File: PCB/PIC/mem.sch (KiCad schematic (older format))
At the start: 14 parts, among them U12 24AA1025, U13 24AA025E48

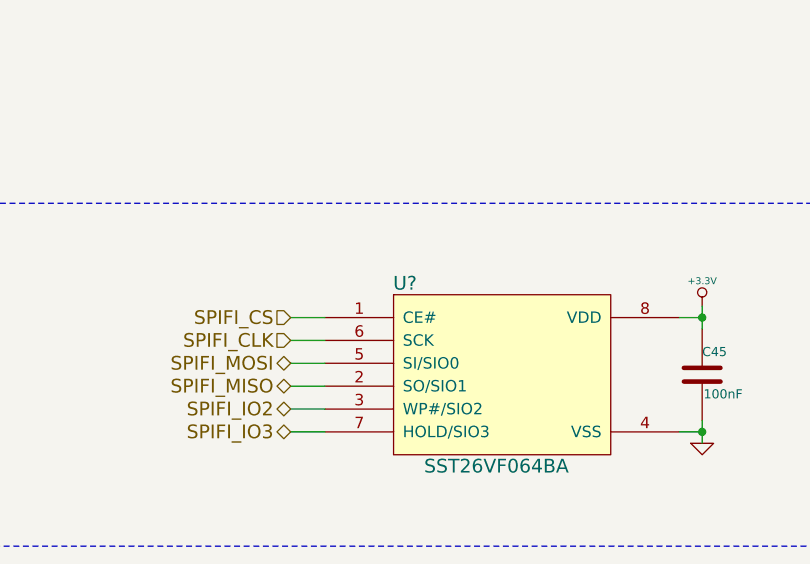
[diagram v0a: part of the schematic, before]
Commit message: CIAA PIC correccion FT232RL
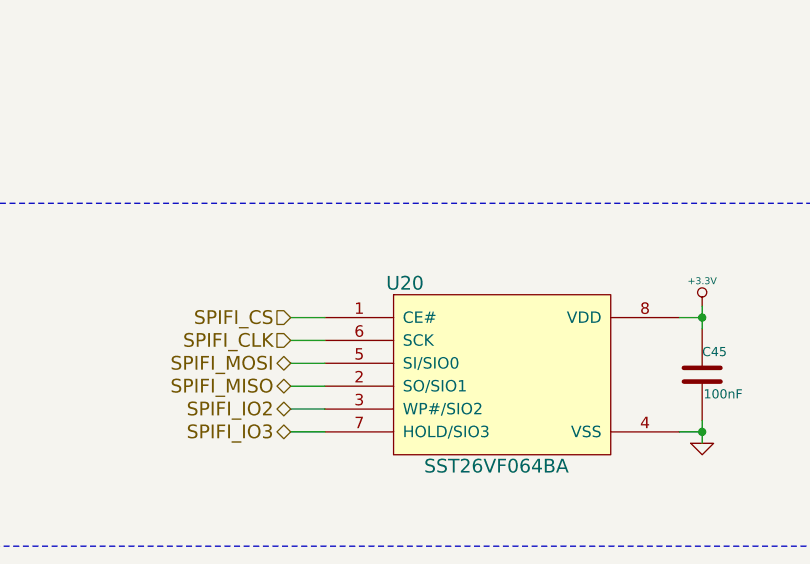
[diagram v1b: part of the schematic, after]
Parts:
- gave numbers to parts that had none: 1
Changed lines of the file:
@@
 Sheet 9 12
 Title "CIAA micro SD card"
-Date "19 dec 2014"
+Date "29 dec 2014"
 Rev "1.0"
 Comp ""
@@
 I2C_SCL
 $Comp
-L GND #PWR164
+L GND #PWR163
 U 1 1 52E536B1
 P 3800 2600
-F 0 "#PWR164" H 3800 2600 30  0001 C CNN
+F 0 "#PWR163" H 3800 2600 30  0001 C CNN
 F 1 "GND" H 3800 2530 30  0001 C CNN
 F 2 "" H 3800 2600 60  0000 C CNN
@@
 $EndComp
 $Comp
-L +3.3V #PWR163
+L +3.3V #PWR162
 U 1 1 52E536B7
 P 3800 1150
-F 0 "#PWR163" H 3800 1110 30  0001 C CNN
+F 0 "#PWR162" H 3800 1110 30  0001 C CNN
 F 1 "+3.3V" H 3800 1260 30  0000 C CNN
 F 2 "" H 3800 1150 60  0000 C CNN
@@
 $EndComp
 $Comp
-L GND #PWR161
+L GND #PWR160
 U 1 1 52E536C5
 P 2850 2600
-F 0 "#PWR161" H 2850 2600 30  0001 C CNN
+F 0 "#PWR160" H 2850 2600 30  0001 C CNN
 F 1 "GND" H 2850 2530 30  0001 C CNN
 F 2 "" H 2850 2600 60  0000 C CNN
@@
 $EndComp
 $Comp
-L GND #PWR160
+L GND #PWR159
 U 1 1 52E536CB
 P 2700 2600
-F 0 "#PWR160" H 2700 2600 30  0001 C CNN
+F 0 "#PWR159" H 2700 2600 30  0001 C CNN
 F 1 "GND" H 2700 2530 30  0001 C CNN
 F 2 "" H 2700 2600 60  0000 C CNN
@@
 $EndComp
 $Comp
-L GND #PWR165
+L GND #PWR164
 U 1 1 52E536D1
 P 4150 1650
-F 0 "#PWR165" H 4150 1650 30  0001 C CNN
+F 0 "#PWR164" H 4150 1650 30  0001 C CNN
 F 1 "GND" H 4150 1580 30  0001 C CNN
 F 2 "" H 4150 1650 60  0000 C CNN
@@
 $EndComp
 $Comp
-L GND #PWR166
+L GND #PWR165
 U 1 1 52E536DF
 P 4850 1550
-F 0 "#PWR166" H 4850 1550 30  0001 C CNN
+F 0 "#PWR165" H 4850 1550 30  0001 C CNN
 F 1 "GND" H 4850 1480 30  0001 C CNN
 F 2 "" H 4850 1550 60  0000 C CNN
@@
 $EndComp
 $Comp
-L +3.3V #PWR162
+L +3.3V #PWR161
 U 1 1 52E536E8
 P 3000 2600
-F 0 "#PWR162" H 3000 2560 30  0001 C CNN
+F 0 "#PWR161" H 3000 2560 30  0001 C CNN
 F 1 "+3.3V" H 3000 2710 30  0000 C CNN
 F 2 "" H 3000 2600 60  0000 C CNN
@@
 I2C_SCL
 $Comp
-L GND #PWR173
+L GND #PWR172
 U 1 1 52E536F8
 P 8100 2600
-F 0 "#PWR173" H 8100 2600 30  0001 C CNN
+F 0 "#PWR172" H 8100 2600 30  0001 C CNN
 F 1 "GND" H 8100 2530 30  0001 C CNN
 F 2 "" H 8100 2600 60  0000 C CNN
@@
 $EndComp
 $Comp
-L +3.3V #PWR172
+L +3.3V #PWR171
 U 1 1 52E536FE
 P 8100 1150
-F 0 "#PWR172" H 8100 1110 30  0001 C CNN
+F 0 "#PWR171" H 8100 1110 30  0001 C CNN
 F 1 "+3.3V" H 8100 1260 30  0000 C CNN
 F 2 "" H 8100 1150 60  0000 C CNN
@@
 $EndComp
 $Comp
-L GND #PWR168
+L GND #PWR169
 U 1 1 52E5370C
 P 7150 2600
-F 0 "#PWR168" H 7150 2600 30  0001 C CNN
+F 0 "#PWR169" H 7150 2600 30  0001 C CNN
 F 1 "GND" H 7150 2530 30  0001 C CNN
 F 2 "" H 7150 2600 60  0000 C CNN
@@
 $EndComp
 $Comp
-L GND #PWR174
+L GND #PWR173
 U 1 1 52E53712
 P 8450 1650
-F 0 "#PWR174" H 8450 1650 30  0001 C CNN
+F 0 "#PWR173" H 8450 1650 30  0001 C CNN
 F 1 "GND" H 8450 1580 30  0001 C CNN
 F 2 "" H 8450 1650 60  0000 C CNN
@@
 $EndComp
 $Comp
-L GND #PWR175
+L GND #PWR174
 U 1 1 52E5371B
 P 9150 1550
-F 0 "#PWR175" H 9150 1550 30  0001 C CNN
+F 0 "#PWR174" H 9150 1550 30  0001 C CNN
 F 1 "GND" H 9150 1480 30  0001 C CNN
 F 2 "" H 9150 1550 60  0000 C CNN
@@
 $EndComp
 $Comp
-L +3.3V #PWR167
+L +3.3V #PWR168
 U 1 1 52E53724
 P 7000 2600
-F 0 "#PWR167" H 7000 2560 30  0001 C CNN
+F 0 "#PWR168" H 7000 2560 30  0001 C CNN
 F 1 "+3.3V" H 7000 2710 30  0000 C CNN
 F 2 "" H 7000 2600 60  0000 C CNN
@@
 $EndComp
 $Comp
-L GND #PWR169
+L GND #PWR170
 U 1 1 52E5372A
 P 7300 2600
-F 0 "#PWR169" H 7300 2600 30  0001 C CNN
+F 0 "#PWR170" H 7300 2600 30  0001 C CNN
 F 1 "GND" H 7300 2530 30  0001 C CNN
 F 2 "" H 7300 2600 60  0000 C CNN
@@
 $EndComp
 $Comp
-L +3.3V #PWR170
+L +3.3V #PWR166
 U 1 1 52E5407E
 P 6700 4300
-F 0 "#PWR170" H 6700 4260 30  0001 C CNN
+F 0 "#PWR166" H 6700 4260 30  0001 C CNN
 F 1 "+3.3V" H 6700 4410 30  0000 C CNN
 F 2 "" H 6700 4300 60  0000 C CNN
@@
 $EndComp
 $Comp
-L GND #PWR171
+L GND #PWR167
 U 1 1 52E540A7
 P 6700 4900
-F 0 "#PWR171" H 6700 4900 30  0001 C CNN
+F 0 "#PWR167" H 6700 4900 30  0001 C CNN
 F 1 "GND" H 6700 4830 30  0001 C CNN
 F 2 "" H 6700 4900 60  0000 C CNN
@@
 Flash QSPI, 64Mbit
 $Comp
-L SST26VF064BA U?
+L SST26VF064BA U20
 U 1 1 5493BBA5
 P 5800 4600
-F 0 "U?" H 5400 5000 60  0000 C CNN
+F 0 "U20" H 5400 5000 60  0000 C CNN
 F 1 "SST26VF064BA" H 5800 4200 60  0000 C CNN
 F 2 "~" H 5800 4400 60  0000 C CNN

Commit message: Correcciones al esquematico segun rev01
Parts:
- added U?: 23A1024, footprints:-SOIC8, symbol 23A1024
- C19, C20, C45: symbol C -> C-RESCUE-ciaa-pic
- R23, R24, R25, R26, R27, R28, R29, R30: symbol R -> R-RESCUE-ciaa-pic
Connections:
- net +3.3V: now also U?.8 (Vcc)
- net GND: now also U?.4 (Vss)
- net SPIFI_CLK: now also U?.6 (SCK)
- net SPIFI_IO2: now also U?.3 (SIO2)
- net SPIFI_IO3: now also U?.7 (HOLD/SIO3)
- net SPIFI_MISO: now also U?.2 (SO/SIO1)
- net SPIFI_MOSI: now also U?.5 (SI/SIO0)
- new net SQICS1: U?.1 (CS)
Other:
- note added: "Aclararía para que esta cada una de las R de 0 Ohm."
- note added: "SRAM - SPI"
- moved on the sheet: C19, C20, C45, R23, R24, R25, R26, R27, R28, R29, R30, U12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

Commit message: rev02, enumeracion componentes JTAG
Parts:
- gave numbers to parts that had none: 1
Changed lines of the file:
@@
 I2C_SCL
 $Comp
-L GND-RESCUE-ciaa-pic #PWR0173
+L GND-RESCUE-ciaa-pic #PWR0174
 U 1 1 52E536B1
 P 5300 3050
-F 0 "#PWR0173" H 5300 3050 30  0001 C CNN
+F 0 "#PWR0174" H 5300 3050 30  0001 C CNN
 F 1 "GND" H 5300 2980 30  0001 C CNN
 F 2 "" H 5300 3050 60  0000 C CNN
@@
 $EndComp
 $Comp
-L +3.3V-RESCUE-ciaa-pic #PWR0174
+L +3.3V-RESCUE-ciaa-pic #PWR0175
 U 1 1 52E536B7
 P 5300 1600
-F 0 "#PWR0174" H 5300 1560 30  0001 C CNN
+F 0 "#PWR0175" H 5300 1560 30  0001 C CNN
 F 1 "+3.3V" H 5300 1710 30  0000 C CNN
 F 2 "" H 5300 1600 60  0000 C CNN
@@
 $EndComp
 $Comp
-L GND-RESCUE-ciaa-pic #PWR0175
+L GND-RESCUE-ciaa-pic #PWR0176
 U 1 1 52E536C5
 P 4350 3050
-F 0 "#PWR0175" H 4350 3050 30  0001 C CNN
+F 0 "#PWR0176" H 4350 3050 30  0001 C CNN
 F 1 "GND" H 4350 2980 30  0001 C CNN
 F 2 "" H 4350 3050 60  0000 C CNN
@@
 $EndComp
 $Comp
-L GND-RESCUE-ciaa-pic #PWR0176
+L GND-RESCUE-ciaa-pic #PWR0177
 U 1 1 52E536CB
 P 4200 3050
-F 0 "#PWR0176" H 4200 3050 30  0001 C CNN
+F 0 "#PWR0177" H 4200 3050 30  0001 C CNN
 F 1 "GND" H 4200 2980 30  0001 C CNN
 F 2 "" H 4200 3050 60  0000 C CNN
@@
 $EndComp
 $Comp
-L GND-RESCUE-ciaa-pic #PWR0177
+L GND-RESCUE-ciaa-pic #PWR0178
 U 1 1 52E536D1
 P 5650 2100
-F 0 "#PWR0177" H 5650 2100 30  0001 C CNN
+F 0 "#PWR0178" H 5650 2100 30  0001 C CNN
 F 1 "GND" H 5650 2030 30  0001 C CNN
 F 2 "" H 5650 2100 60  0000 C CNN
@@
 $EndComp
 $Comp
-L GND-RESCUE-ciaa-pic #PWR0178
+L GND-RESCUE-ciaa-pic #PWR0179
 U 1 1 52E536DF
 P 6350 2000
-F 0 "#PWR0178" H 6350 2000 30  0001 C CNN
+F 0 "#PWR0179" H 6350 2000 30  0001 C CNN
 F 1 "GND" H 6350 1930 30  0001 C CNN
 F 2 "" H 6350 2000 60  0000 C CNN
@@
 $EndComp
 $Comp
-L +3.3V-RESCUE-ciaa-pic #PWR0179
+L +3.3V-RESCUE-ciaa-pic #PWR0180
 U 1 1 52E536E8
 P 4500 3050
-F 0 "#PWR0179" H 4500 3010 30  0001 C CNN
+F 0 "#PWR0180" H 4500 3010 30  0001 C CNN
 F 1 "+3.3V" H 4500 3160 30  0000 C CNN
 F 2 "" H 4500 3050 60  0000 C CNN
@@
 I2C_SCL
 $Comp
-L GND-RESCUE-ciaa-pic #PWR0180
+L GND-RESCUE-ciaa-pic #PWR0181
 U 1 1 52E536F8
 P 8900 3050
-F 0 "#PWR0180" H 8900 3050 30  0001 C CNN
+F 0 "#PWR0181" H 8900 3050 30  0001 C CNN
 F 1 "GND" H 8900 2980 30  0001 C CNN
 F 2 "" H 8900 3050 60  0000 C CNN
@@
 $EndComp
 $Comp
-L +3.3V-RESCUE-ciaa-pic #PWR0181
+L +3.3V-RESCUE-ciaa-pic #PWR0182
 U 1 1 52E536FE
 P 8900 1600
-F 0 "#PWR0181" H 8900 1560 30  0001 C CNN
+F 0 "#PWR0182" H 8900 1560 30  0001 C CNN
 F 1 "+3.3V" H 8900 1710 30  0000 C CNN
 F 2 "" H 8900 1600 60  0000 C CNN
@@
 $EndComp
 $Comp
-L GND-RESCUE-ciaa-pic #PWR0182
+L GND-RESCUE-ciaa-pic #PWR0183
 U 1 1 52E5370C
 P 7950 3050
-F 0 "#PWR0182" H 7950 3050 30  0001 C CNN
+F 0 "#PWR0183" H 7950 3050 30  0001 C CNN
 F 1 "GND" H 7950 2980 30  0001 C CNN
 F 2 "" H 7950 3050 60  0000 C CNN
@@
 $EndComp
 $Comp
-L GND-RESCUE-ciaa-pic #PWR0183
+L GND-RESCUE-ciaa-pic #PWR0184
 U 1 1 52E53712
 P 9250 2100
-F 0 "#PWR0183" H 9250 2100 30  0001 C CNN
+F 0 "#PWR0184" H 9250 2100 30  0001 C CNN
 F 1 "GND" H 9250 2030 30  0001 C CNN
 F 2 "" H 9250 2100 60  0000 C CNN
@@
 $EndComp
 $Comp
-L GND-RESCUE-ciaa-pic #PWR0184
+L GND-RESCUE-ciaa-pic #PWR0185
 U 1 1 52E5371B
 P 9950 2000
-F 0 "#PWR0184" H 9950 2000 30  0001 C CNN
+F 0 "#PWR0185" H 9950 2000 30  0001 C CNN
 F 1 "GND" H 9950 1930 30  0001 C CNN
 F 2 "" H 9950 2000 60  0000 C CNN
@@
 $EndComp
 $Comp
-L +3.3V-RESCUE-ciaa-pic #PWR0185
+L +3.3V-RESCUE-ciaa-pic #PWR0186
 U 1 1 52E53724
 P 7800 3050
-F 0 "#PWR0185" H 7800 3010 30  0001 C CNN
+F 0 "#PWR0186" H 7800 3010 30  0001 C CNN
 F 1 "+3.3V" H 7800 3160 30  0000 C CNN
 F 2 "" H 7800 3050 60  0000 C CNN
@@
 $EndComp
 $Comp
-L GND-RESCUE-ciaa-pic #PWR0186
+L GND-RESCUE-ciaa-pic #PWR0187
 U 1 1 52E5372A
 P 8100 3050
-F 0 "#PWR0186" H 8100 3050 30  0001 C CNN
+F 0 "#PWR0187" H 8100 3050 30  0001 C CNN
 F 1 "GND" H 8100 2980 30  0001 C CNN
 F 2 "" H 8100 3050 60  0000 C CNN
@@
 $EndComp
 $Comp
-L +3.3V-RESCUE-ciaa-pic #PWR0187
+L +3.3V-RESCUE-ciaa-pic #PWR0188
 U 1 1 52E5407E
 P 6700 4950
-F 0 "#PWR0187" H 6700 4910 30  0001 C CNN
+F 0 "#PWR0188" H 6700 4910 30  0001 C CNN
 F 1 "+3.3V" H 6700 5060 30  0000 C CNN
 F 2 "" H 6700 4950 60  0000 C CNN
@@
 $EndComp
 $Comp
-L GND-RESCUE-ciaa-pic #PWR0188
+L GND-RESCUE-ciaa-pic #PWR0189
 U 1 1 52E540A7
 P 6700 5550
-F 0 "#PWR0188" H 6700 5550 30  0001 C CNN
+F 0 "#PWR0189" H 6700 5550 30  0001 C CNN
 F 1 "GND" H 6700 5480 30  0001 C CNN
 F 2 "" H 6700 5550 60  0000 C CNN
@@
 Aclararía para que esta cada una de las R de 0 Ohm.
 $Comp
-L 23A1024 U?
+L 23A1024 U24
 U 1 1 577B0CDB
 P 2000 2300
-F 0 "U?" H 2150 1800 60  0000 C CNN
+F 0 "U24" H 2150 1800 60  0000 C CNN
 F 1 "23A1024" H 1750 2750 60  0000 C CNN
 F 2 "footprints:-SOIC8" H 1450 1700 60  0001 C CNN
@@
 $EndComp
 $Comp
-L GND-RESCUE-ciaa-pic #PWR?
+L GND-RESCUE-ciaa-pic #PWR0190
 U 1 1 577B0CE8
 P 2000 3200
-F 0 "#PWR?" H 2000 3200 30  0001 C CNN
+F 0 "#PWR0190" H 2000 3200 30  0001 C CNN
 F 1 "GND" H 2000 3130 30  0001 C CNN
 F 2 "" H 2000 3200 60  0000 C CNN
@@
 $EndComp
 $Comp
-L +3.3V-RESCUE-ciaa-pic #PWR?
+L +3.3V-RESCUE-ciaa-pic #PWR0191
 U 1 1 577B0CEE
 P 2000 1500
-F 0 "#PWR?" H 2000 1460 30  0001 C CNN
+F 0 "#PWR0191" H 2000 1460 30  0001 C CNN
 F 1 "+3.3V" H 2000 1610 30  0000 C CNN
 F 2 "" H 2000 1500 60  0000 C CNN
